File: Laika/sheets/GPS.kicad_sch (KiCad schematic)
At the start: 9 parts, among them J8 Conn_01x05, U6 SAM-M8Q

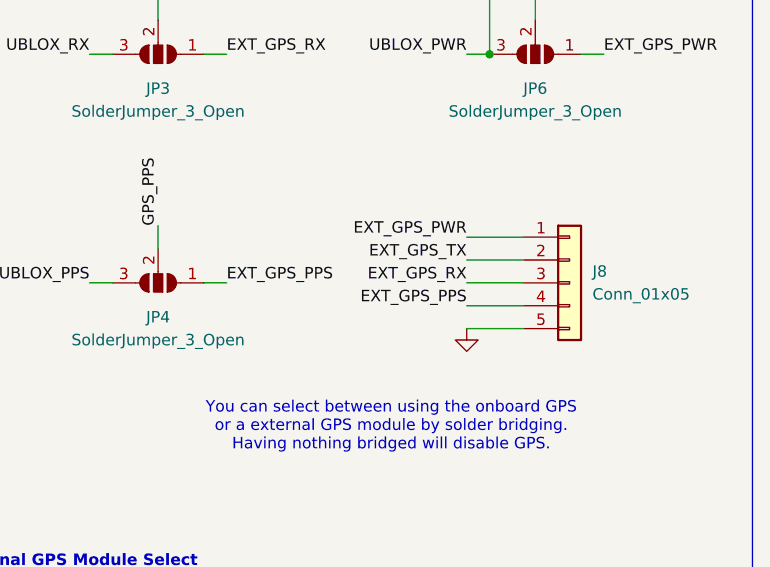
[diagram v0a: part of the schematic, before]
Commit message: Populated BOM with part numbers and footprints
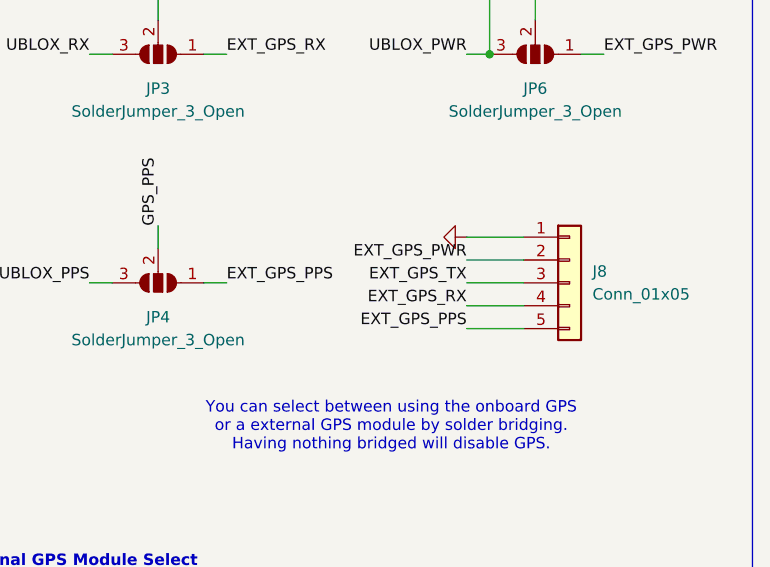
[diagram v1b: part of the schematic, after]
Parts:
- J8: footprint (none) -> Connector_PinHeader_1.00mm:PinHeader_1x05_P1.00mm_Vertical
- R28, R29: footprint (none) -> Resistor_SMD:R_0402_1005Metric_Pad0.72x0.64mm_HandSolder
- U6: JLC Part Type (none) -> Extended; Manafacturer (none) -> u-blox; Part Number (none) -> SAM-M8Q-0
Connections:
- net EXT_GPS_PPS: now also J8.5 (Pin_5); no longer J8.4 (Pin_4)
- net EXT_GPS_PWR: now also J8.2 (Pin_2); no longer J8.1 (Pin_1)
- net EXT_GPS_RX: now also J8.4 (Pin_4); no longer J8.3 (Pin_3)
- net EXT_GPS_TX: now also J8.3 (Pin_3); no longer J8.2 (Pin_2)
- net GND: now also J8.1 (Pin_1); no longer J8.5 (Pin_5)

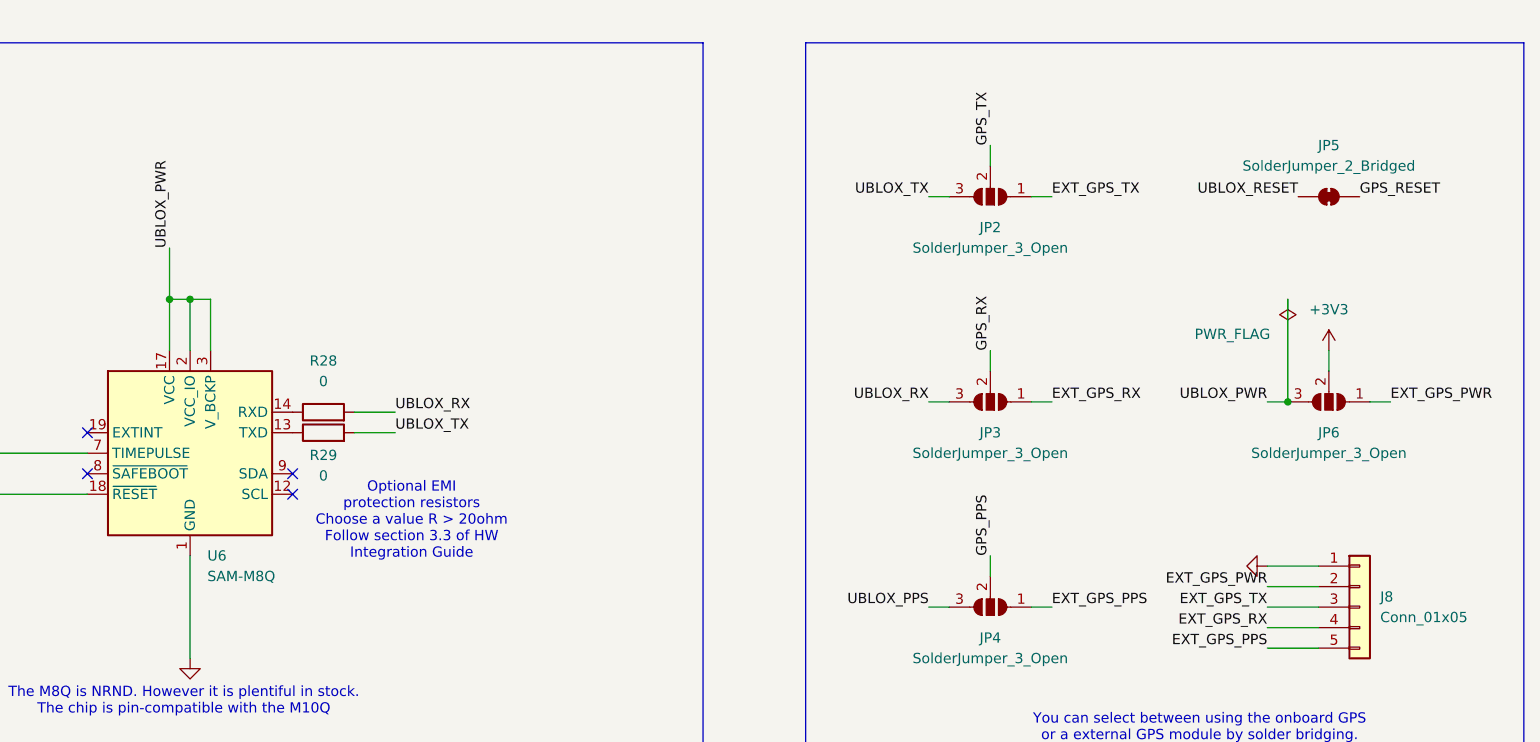
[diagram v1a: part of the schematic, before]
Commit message: Removed external GPS power.
GPS (on board and external) are powered by the 3V3 power rail.
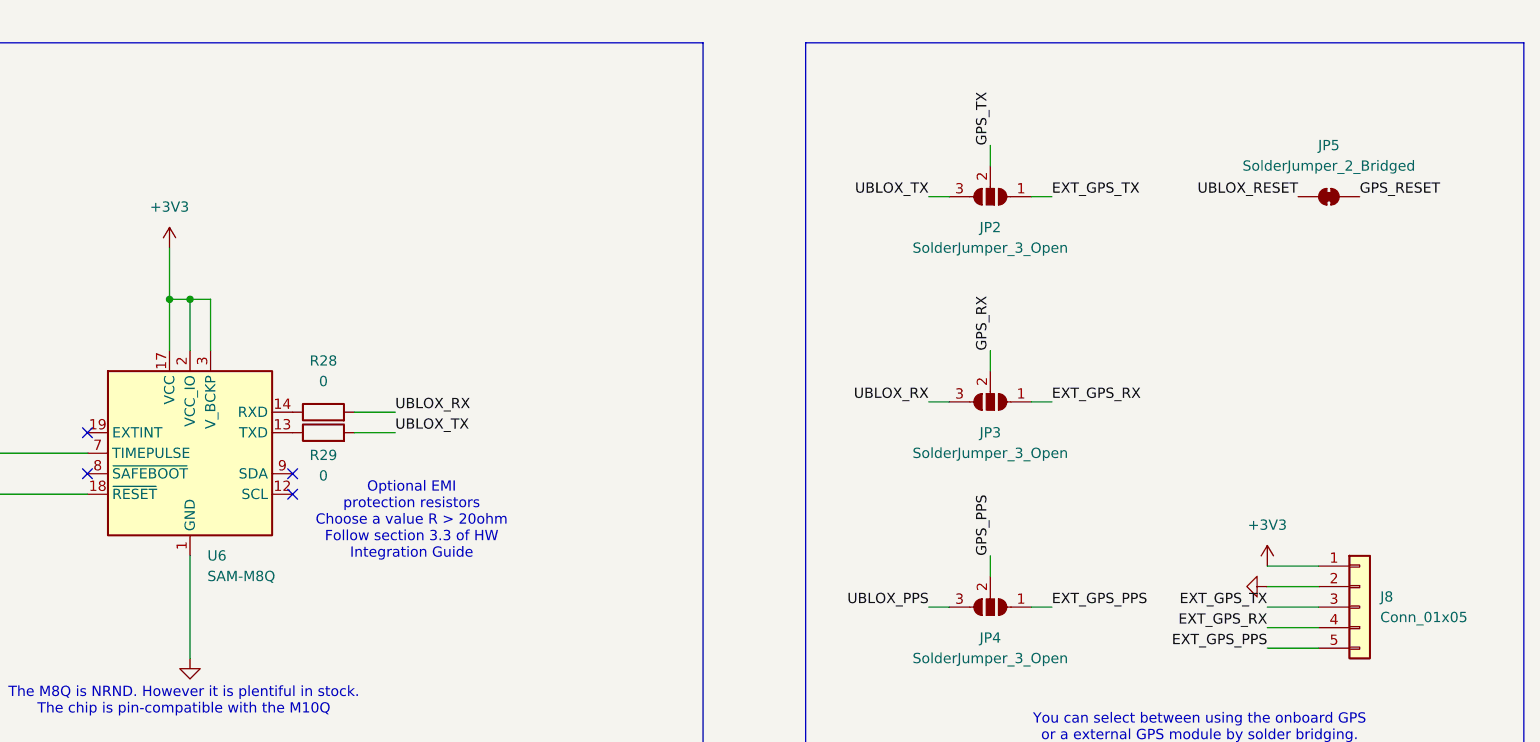
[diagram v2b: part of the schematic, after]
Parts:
- removed JP6: SolderJumper_3_Open, Jumper:SolderJumper-3_P1.3mm_Open_Pad1.0x1.5mm, symbol Jumper:SolderJumper_3_Open
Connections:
- net EXT_GPS_PWR is gone; now on net GND: J8.2 (Pin_2)
- net UBLOX_PWR is gone; now on net +3V3: U6.17 (VCC), U6.2 (VCC_IO), U6.3 (V_BCKP)
- net +3V3: now also J8.1 (Pin_1)
- net GND: no longer J8.1 (Pin_1)
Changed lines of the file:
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@@
-	)
-	(junction
-		(at 237.49 82.55)
-		(diameter 0)
-		(color 0 0 0 0)
 	)
 	(junction
@@
 	(wire
 		(pts
-			(xy 234.95 82.55) (xy 237.49 82.55)
-		)
-		(stroke
-			(width 0)
-			(type default)
-		)
-	)
-	(wire
-		(pts
 			(xy 200.66 101.6) (xy 200.66 104.14)
 		)
@@
 	(wire
 		(pts
-			(xy 242.57 76.2) (xy 242.57 78.74)
-		)
-		(stroke
-			(width 0)
-			(type default)
-		)
-	)
-	(wire
-		(pts
 			(xy 200.66 50.8) (xy 200.66 53.34)
 		)
@@
 	(wire
 		(pts
-			(xy 237.49 69.85) (xy 237.49 82.55)
-		)
-		(stroke
-			(width 0)
-			(type default)
-		)
-	)
-	(wire
-		(pts
 			(xy 88.9 175.26) (xy 99.06 175.26)
 		)
@@
 		(pts
 			(xy 76.2 88.9) (xy 88.9 88.9)
-		)
-		(stroke
-			(width 0)
-			(type default)
-		)
-	)
-	(wire
-		(pts
-			(xy 250.19 82.55) (xy 247.65 82.55)
 		)
 		(stroke
@@
 		)
 	)
-	(label "EXT_GPS_PWR"
-		(at 250.19 82.55 0)
-		(effects
-			(font
-				(size 1.27 1.27)
-			)
-			(justify left bottom)
-		)
-	)
 	(label "UBLOX_RX"
 		(at 193.04 82.55 180)
@@
 		)
 	)
-	(label "EXT_GPS_PWR"
-		(at 234.95 105.41 180)
-		(effects
-			(font
-				(size 1.27 1.27)
-			)
-			(justify right bottom)
-		)
-	)
-	(label "UBLOX_PWR"
-		(at 234.95 82.55 180)
-		(effects
-			(font
-				(size 1.27 1.27)
-			)
-			(justify right bottom)
-		)
-	)
 	(label "GPS_TX"
 		(at 200.66 50.8 90)
-		(effects
-			(font
-				(size 1.27 1.27)
-			)
-			(justify left bottom)
-		)
-	)
-	(label "UBLOX_PWR"
-		(at 99.06 63.5 90)
 		(effects
 			(font
@@
 			)
 			(justify left)
-		)
-	)
-	(symbol
-		(lib_id "Jumper:SolderJumper_3_Open")
-		(at 242.57 82.55 180)
-		(unit 1)
-		(exclude_from_sim no)
-		(in_bom no)
-		(on_board yes)
-		(dnp no)
-		(fields_autoplaced yes)
-		(property "Reference" "JP6"
-			(at 242.57 86.36 0)
-			(effects
-				(font
-					(size 1.27 1.27)
-				)
-			)
-		)
-		(property "Value" "SolderJumper_3_Open"
-			(at 242.57 88.9 0)
-			(effects
-				(font
-					(size 1.27 1.27)
-				)
-			)
-		)
-		(property "Footprint" "Jumper:SolderJumper-3_P1.3mm_Open_Pad1.0x1.5mm"
-			(at 242.57 82.55 0)
-			(effects
-				(font
-					(size 1.27 1.27)
-				)
-				(hide yes)
-			)
-		)
-		(property "Datasheet" "~"
-			(at 242.57 82.55 0)
-			(effects
-				(font
-					(size 1.27 1.27)
-				)
-				(hide yes)
-			)
-		)
-		(property "Description" "Solder Jumper, 3-pole, open"
-			(at 242.57 82.55 0)
-			(effects
-				(font
-					(size 1.27 1.27)
-				)
-				(hide yes)
-			)
-		)
-		(pin "1"
-		)
-		(pin "3"
-		)
-		(pin "2"
-		)
-		(instances
-			(project "Laika"
-				(path "/57baccbf-5d29-4714-8f2e-7e9f593fcdf8/6c078d98-f795-4bff-ba6d-ace5d579e960/2a1083d0-6c48-490a-b311-5d9ae5229ae7"
-					(reference "JP6")
-					(unit 1)
-				)
-			)
 		)
 	)
@@
 	)
 	(symbol
+		(lib_id "power:+3V3")
+		(at 99.06 63.5 0)
+		(unit 1)
+		(exclude_from_sim no)
+		(in_bom yes)
+		(on_board yes)
+		(dnp no)
+		(fields_autoplaced yes)
+		(property "Reference" "#PWR086"
+			(at 99.06 67.31 0)
+			(effects
+				(font
+					(size 1.27 1.27)
+				)
+				(hide yes)
+			)
+		)
+		(property "Value" "+3V3"
+			(at 99.06 58.42 0)
+			(effects
+				(font
+					(size 1.27 1.27)
+				)
+			)
+		)
+		(property "Footprint" ""
+			(at 99.06 63.5 0)
+			(effects
+				(font
+					(size 1.27 1.27)
+				)
+				(hide yes)
+			)
+		)
+		(property "Datasheet" ""
+			(at 99.06 63.5 0)
+			(effects
+				(font
+					(size 1.27 1.27)
+				)
+				(hide yes)
+			)
+		)
+		(property "Description" "Power symbol creates a global label with name \"+3V3\""
+			(at 99.06 63.5 0)
+			(effects
+				(font
+					(size 1.27 1.27)
+				)
+				(hide yes)
+			)
+		)
+		(pin "1"
+		)
+		(instances
+			(project ""
+				(path "/57baccbf-5d29-4714-8f2e-7e9f593fcdf8/6c078d98-f795-4bff-ba6d-ace5d579e960/2a1083d0-6c48-490a-b311-5d9ae5229ae7"
+					(reference "#PWR086")
+					(unit 1)
+				)
+			)
+		)
+	)
+	(symbol
 		(lib_id "power:GND")
-		(at 234.95 102.87 270)
+		(at 234.95 105.41 270)
 		(unit 1)
 		(exclude_from_sim no)
@@
 		(fields_autoplaced yes)
 		(property "Reference" "#PWR084"
-			(at 228.6 102.87 0)
+			(at 228.6 105.41 0)
 			(effects
 				(font
@@
 		)
 		(property "Value" "GND"
-			(at 229.87 102.87 0)
+			(at 229.87 105.41 0)
 			(effects
 				(font
@@
 		)
 		(property "Footprint" ""
-			(at 234.95 102.87 0)
+			(at 234.95 105.41 0)
 			(effects
 				(font
@@
 		)
 		(property "Datasheet" ""
-			(at 234.95 102.87 0)
+			(at 234.95 105.41 0)
 			(effects
 				(font
@@
 		)
 		(property "Description" "Power symbol creates a global label with name \"GND\" , ground"
-			(at 234.95 102.87 0)
+			(at 234.95 105.41 0)
 			(effects
 				(font
@@
 	(symbol
 		(lib_id "power:+3V3")
-		(at 242.57 76.2 0)
+		(at 234.95 102.87 0)
 		(unit 1)
 		(exclude_from_sim no)
@@
 		(dnp no)
 		(fields_autoplaced yes)
-		(property "Reference" "#PWR086"
-			(at 242.57 80.01 0)
+		(property "Reference" "#PWR0109"
+			(at 234.95 106.68 0)
 			(effects
 				(font
@@
 		)
 		(property "Value" "+3V3"
-			(at 242.57 71.12 0)
+			(at 234.95 97.79 0)
 			(effects
 				(font
@@
 		)
 		(property "Footprint" ""
-			(at 242.57 76.2 0)
+			(at 234.95 102.87 0)
 			(effects
 				(font
@@
 		)
 		(property "Datasheet" ""
-			(at 242.57 76.2 0)
+			(at 234.95 102.87 0)
 			(effects
 				(font
@@
 		)
 		(property "Description" "Power symbol creates a global label with name \"+3V3\""
-			(at 242.57 76.2 0)
+			(at 234.95 102.87 0)
 			(effects
 				(font
@@
 		)
 		(instances
-			(project ""
+			(project "Laika"
 				(path "/57baccbf-5d29-4714-8f2e-7e9f593fcdf8/6c078d98-f795-4bff-ba6d-ace5d579e960/2a1083d0-6c48-490a-b311-5d9ae5229ae7"
-					(reference "#PWR086")
+					(reference "#PWR0109")
 					(unit 1)
 				)
@@
 					(unit 1)
 				)
-			)
-		)
-	)
-	(symbol
-		(lib_id "power:PWR_FLAG")
-		(at 237.49 69.85 180)
-		(unit 1)
-		(exclude_from_sim no)
-		(in_bom yes)
-		(on_board yes)
-		(dnp no)
-		(property "Reference" "#FLG08"
-			(at 237.49 71.755 0)
-			(effects
-				(font
-					(size 1.27 1.27)
-				)
-				(hide yes)
-			)
-		)
-		(property "Value" "PWR_FLAG"
-			(at 230.632 74.168 0)
-			(effects
-				(font
-					(size 1.27 1.27)
-				)
-			)
-		)
-		(property "Footprint" ""
-			(at 237.49 69.85 0)
-			(effects
-				(font
-					(size 1.27 1.27)
-				)
-				(hide yes)
-			)
-		)
-		(property "Datasheet" "~"
-			(at 237.49 69.85 0)
-			(effects
-				(font
-					(size 1.27 1.27)
-				)
-				(hide yes)
-			)
-		)
-		(property "Description" "Special symbol for telling ERC where power comes from"
-			(at 237.49 69.85 0)
-			(effects
-				(font
-					(size 1.27 1.27)
-				)
-				(hide yes)
-			)
-		)
-		(pin "1"
-		)
-		(instances
-			(project ""
-				(path "/57baccbf-5d29-4714-8f2e-7e9f593fcdf8/6c078d98-f795-4bff-ba6d-ace5d579e960/2a1083d0-6c48-490a-b311-5d9ae5229ae7"
-					(reference "#FLG08")
-					(unit 1)
-				)
